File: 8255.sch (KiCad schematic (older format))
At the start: 2 parts

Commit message: updated pins instead of busses
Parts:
- added J1: DB25_Female, symbol Connector:DB25_Female
- gave numbers to parts that had none: 2
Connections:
- net labels added: A10, A11, A12, A13, A14, A15, A3, A4, A5, A6, A7, A8, A9, D0, D1, D2, D3, D4, D5, D6, D7, P0, P1, P10, P11, P12, P13, P14, P15, P16, P17, P18, P19, P2, P20, P21, P22, P23, P24, P3, P4, P5, P6, P7, P8, P9
- net labels removed: A[2:15], D[0:7], PA[0:7], PB[0:7], PC[0:7]
- wire segments 63 -> 80

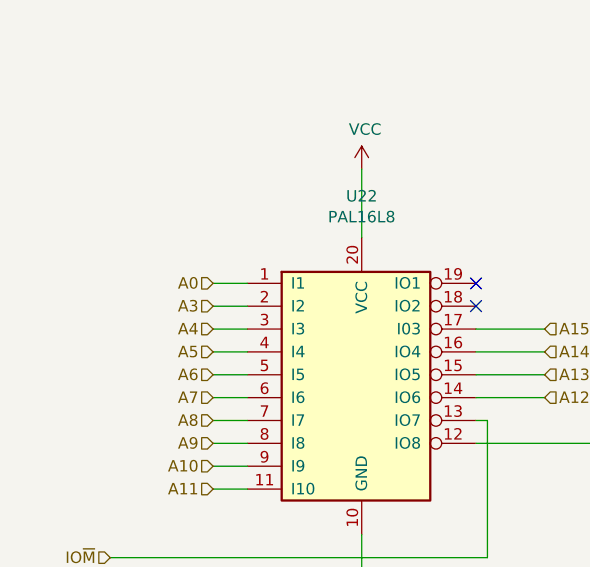
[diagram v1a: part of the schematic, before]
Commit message: added A2
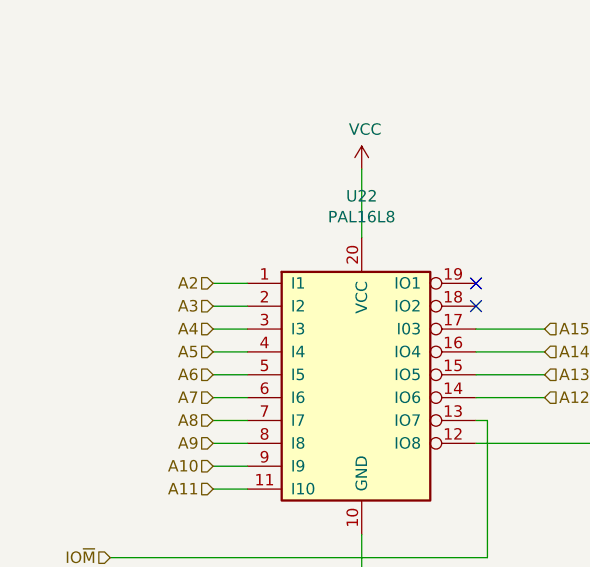
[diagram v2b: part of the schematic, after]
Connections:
- net labels added: A2
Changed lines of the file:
@@
 	1450 3200 1300 3200
 Text HLabel 1300 3200 0    50   Input ~ 0
-A0
+A2
 Text HLabel 1300 3300 0    50   Input ~ 0
 A3

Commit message: 3 chips
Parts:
- removed J1: DB25_Female, symbol Connector:DB25_Female
- added J? (x9): Conn_01x08_Female, symbol Connector:Conn_01x08_Female
- added U? (x2): 8255, Package_DIP:DIP-40_W15.24mm, symbol Interface:8255
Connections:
- net labels added: P25, P26, P27, P28, P29, P30, P31, P32, P33, P34, P35, P36, P37, P38, P39, P40, P41, P42, P43, P44, P45, P46, P47, P48, P49, P50, P51, P52, P53, P54, P55, P56, P57, P58, P59, P60, P61, P62, P63, P64, P65, P66, P67, P68, P69, P70, P71
- wire segments 80 -> 130
- no-connect marks 2 -> 0
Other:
- moved on the sheet: U22

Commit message: annotations
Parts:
- gave numbers to parts that had none: 11
- renumbered U23 to PPI1, U22 to PPI_Decoder
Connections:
- wire segments 130 -> 149
